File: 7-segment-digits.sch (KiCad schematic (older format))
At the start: 0 parts

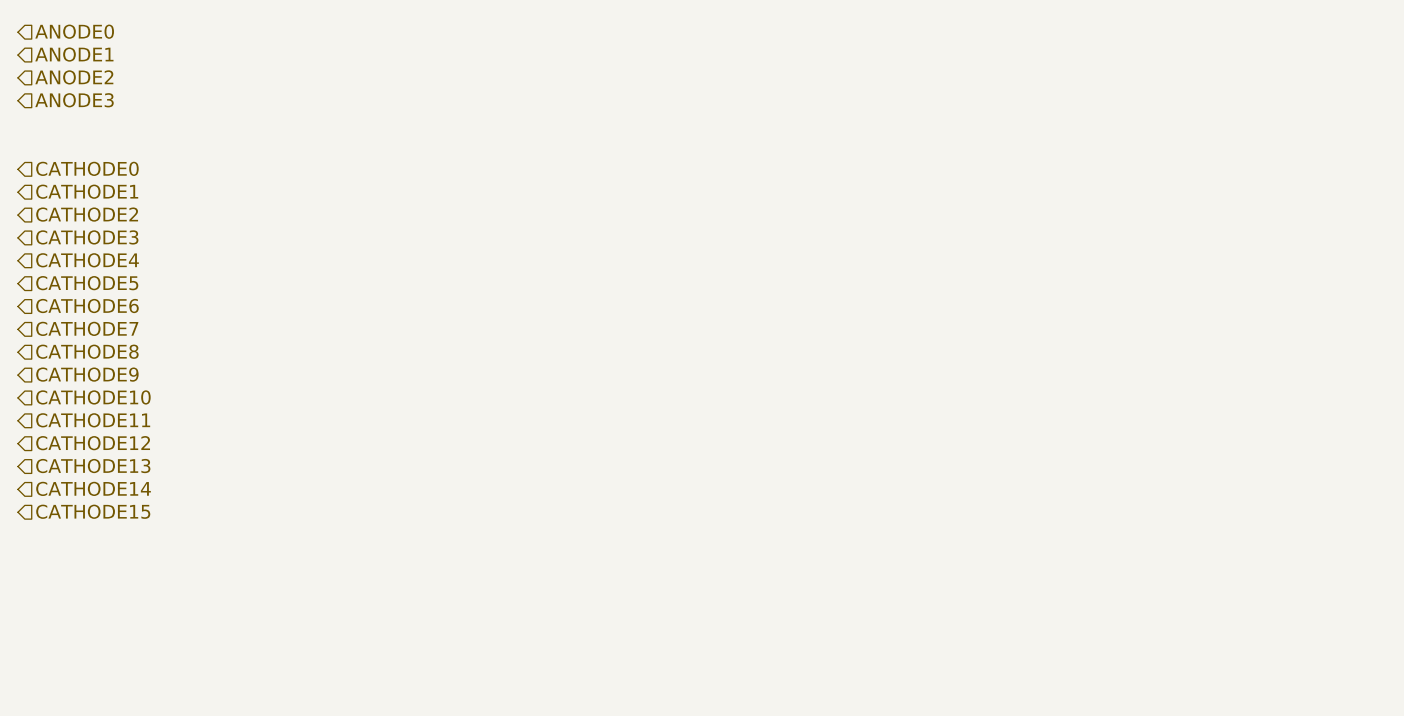
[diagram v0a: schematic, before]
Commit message: I think the layout is finished now. I'll check again after I sleep.
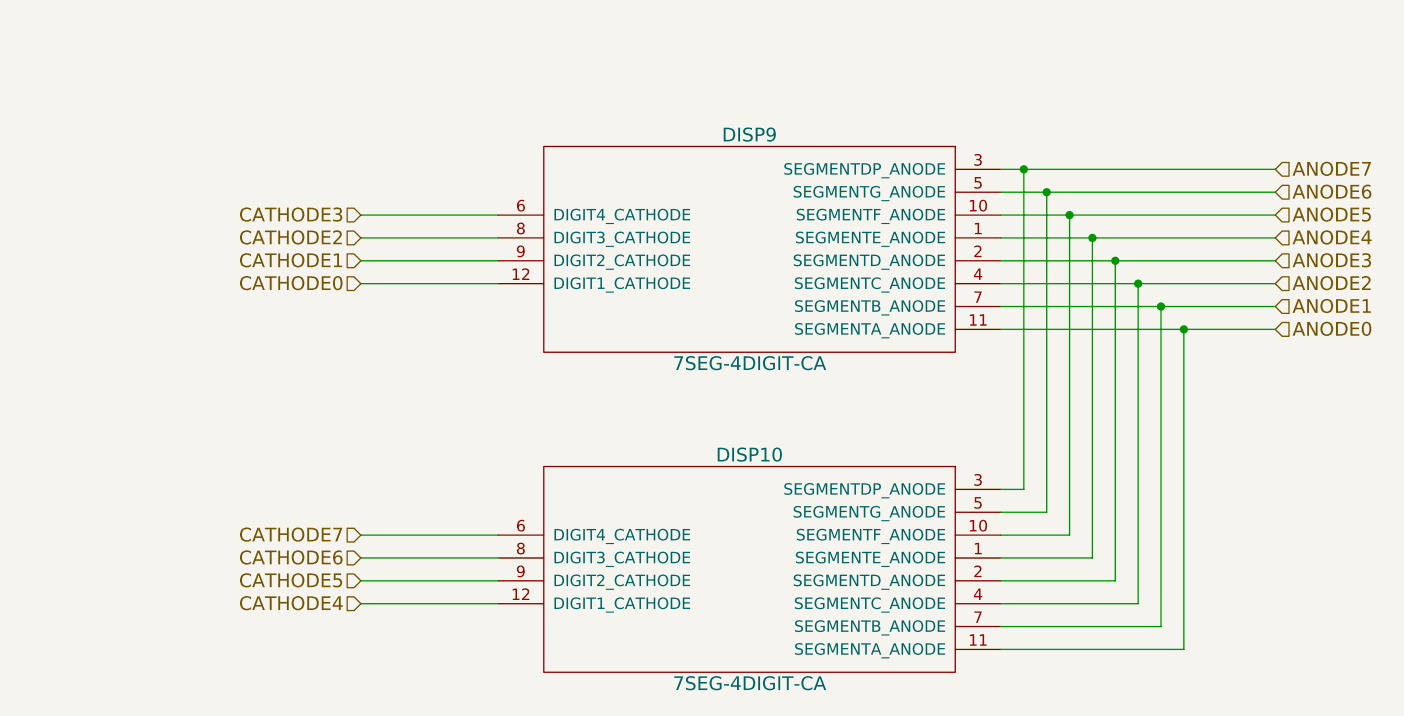
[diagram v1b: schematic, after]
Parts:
- added DISP10, DISP9: 7SEG-4DIGIT-CA, PinballParts:ATA8041, symbol 7SEG-4DIGIT-CA
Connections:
- net ANODE0: now also DISP10.11 (SEGMENTA_ANODE), DISP9.11 (SEGMENTA_ANODE)
- net ANODE1: now also DISP10.7 (SEGMENTB_ANODE), DISP9.7 (SEGMENTB_ANODE)
- net ANODE2: now also DISP10.4 (SEGMENTC_ANODE), DISP9.4 (SEGMENTC_ANODE)
- net ANODE3: now also DISP10.2 (SEGMENTD_ANODE), DISP9.2 (SEGMENTD_ANODE)
- net CATHODE0: now also DISP9.12 (DIGIT1_CATHODE)
- net CATHODE1: now also DISP9.9 (DIGIT2_CATHODE)
- net CATHODE2: now also DISP9.8 (DIGIT3_CATHODE)
- net CATHODE3: now also DISP9.6 (DIGIT4_CATHODE)
- net CATHODE4: now also DISP10.12 (DIGIT1_CATHODE)
- net CATHODE5: now also DISP10.9 (DIGIT2_CATHODE)
- net CATHODE6: now also DISP10.8 (DIGIT3_CATHODE)
- net CATHODE7: now also DISP10.6 (DIGIT4_CATHODE)
- new net ANODE4: DISP10.1 (SEGMENTE_ANODE), DISP9.1 (SEGMENTE_ANODE)
- new net ANODE5: DISP10.10 (SEGMENTF_ANODE), DISP9.10 (SEGMENTF_ANODE)
- new net ANODE6: DISP10.5 (SEGMENTG_ANODE), DISP9.5 (SEGMENTG_ANODE)
- new net ANODE7: DISP10.3 (SEGMENTDP_ANODE), DISP9.3 (SEGMENTDP_ANODE)
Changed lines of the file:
@@
 EESchema Schematic File Version 2
+LIBS:score-module-pcb-v1-rescue
 LIBS:power
 LIBS:device
@@
 LIBS:memory
 LIBS:xilinx
-LIBS:special
 LIBS:microcontrollers
 LIBS:dsp
@@
 Comment4 ""
 $EndDescr
-Text HLabel 2600 1800 2    60   Input ~ 0
+Text HLabel 8100 3100 2    60   Input ~ 0
 ANODE0
-Text HLabel 2600 1900 2    60   Input ~ 0
+Text HLabel 8100 3000 2    60   Input ~ 0
 ANODE1
-Text HLabel 2600 2000 2    60   Input ~ 0
+Text HLabel 8100 2900 2    60   Input ~ 0
 ANODE2
-Text HLabel 2600 2100 2    60   Input ~ 0
+Text HLabel 8100 2800 2    60   Input ~ 0
 ANODE3
-Text HLabel 2600 2400 2    60   Input ~ 0
+Text HLabel 4100 2900 0    60   Input ~ 0
 CATHODE0
-Text HLabel 2600 2500 2    60   Input ~ 0
+Text HLabel 4100 2800 0    60   Input ~ 0
 CATHODE1
-Text HLabel 2600 2600 2    60   Input ~ 0
+Text HLabel 4100 2700 0    60   Input ~ 0
 CATHODE2
-Text HLabel 2600 2700 2    60   Input ~ 0
+Text HLabel 4100 2600 0    60   Input ~ 0
 CATHODE3
-Text HLabel 2600 2800 2    60   Input ~ 0
+Text HLabel 4100 4300 0    60   Input ~ 0
 CATHODE4
-Text HLabel 2600 2900 2    60   Input ~ 0
+Text HLabel 4100 4200 0    60   Input ~ 0
 CATHODE5
-Text HLabel 2600 3000 2    60   Input ~ 0
+Text HLabel 4100 4100 0    60   Input ~ 0
 CATHODE6
-Text HLabel 2600 3100 2    60   Input ~ 0
+Text HLabel 4100 4000 0    60   Input ~ 0
 CATHODE7
-Text HLabel 2600 3200 2    60   Input ~ 0
-CATHODE8
-Text HLabel 2600 3300 2    60   Input ~ 0
-CATHODE9
-Text HLabel 2600 3400 2    60   Input ~ 0
-CATHODE10
-Text HLabel 2600 3500 2    60   Input ~ 0
-CATHODE11
-Text HLabel 2600 3600 2    60   Input ~ 0
-CATHODE12
-Text HLabel 2600 3700 2    60   Input ~ 0
-CATHODE13
-Text HLabel 2600 3800 2    60   Input ~ 0
-CATHODE14
-Text HLabel 2600 3900 2    60   Input ~ 0
-CATHODE15
+Text HLabel 8100 2700 2    60   Input ~ 0
+ANODE4
+Text HLabel 8100 2600 2    60   Input ~ 0
+ANODE5
+Text HLabel 8100 2500 2    60   Input ~ 0
+ANODE6
+Text HLabel 8100 2400 2    60   Input ~ 0
+ANODE7
+$Comp
+L 7SEG-4DIGIT-CA DISP9
+U 1 1 560EA1A5
+P 5800 2750
+F 0 "DISP9" H 5800 3250 60  0000 C CNN
+F 1 "7SEG-4DIGIT-CA" H 5800 2250 60  0000 C CNN
+F 2 "PinballParts:ATA8041" H 5800 2750 60  0001 C CNN
+F 3 "" H 5800 2750 60  0000 C CNN
+	1    5800 2750
+	1    0    0    -1
+$EndComp
+$Comp
+L 7SEG-4DIGIT-CA DISP10
+U 1 1 560EA1DC
+P 5800 4150
+F 0 "DISP10" H 5800 4650 60  0000 C CNN
+F 1 "7SEG-4DIGIT-CA" H 5800 3650 60  0000 C CNN
+F 2 "PinballParts:ATA8041" H 5800 4150 60  0001 C CNN
+F 3 "" H 5800 4150 60  0000 C CNN
+	1    5800 4150
+	1    0    0    -1
+$EndComp
+Wire Wire Line
+	8100 3100 6900 3100
+Wire Wire Line
+	6900 3000 8100 3000
+Wire Wire Line
+	8100 2900 6900 2900
+Wire Wire Line
+	6900 2800 8100 2800
+Wire Wire Line
+	8100 2700 6900 2700
+Wire Wire Line
+	6900 2600 8100 2600
+Wire Wire Line
+	8100 2500 6900 2500
+Wire Wire Line
+	6900 2400 8100 2400
+Wire Wire Line
+	6900 3800 7000 3800
+Wire Wire Line
+	7000 3800 7000 2400
+Connection ~ 7000 2400
+Wire Wire Line
+	6900 3900 7100 3900
+Wire Wire Line
+	7100 3900 7100 2500
+Connection ~ 7100 2500
+Wire Wire Line
+	7200 2600 7200 4000
+Wire Wire Line
+	7200 4000 6900 4000
+Connection ~ 7200 2600
+Wire Wire Line
+	6900 4100 7300 4100
+Wire Wire Line
+	7300 4100 7300 2700
+Connection ~ 7300 2700
+Wire Wire Line
+	7400 2800 7400 4200
+Wire Wire Line
+	7400 4200 6900 4200
+Connection ~ 7400 2800
+Wire Wire Line
+	6900 4300 7500 4300
+Wire Wire Line
+	7500 4300 7500 2900
+Connection ~ 7500 2900
+Wire Wire Line
+	6900 4400 7600 4400
+Wire Wire Line
+	7600 4400 7600 3000
+Connection ~ 7600 3000
+Wire Wire Line
+	6900 4500 7700 4500
+Wire Wire Line
+	7700 4500 7700 3100
+Connection ~ 7700 3100
+Wire Wire Line
+	4700 4300 4100 4300
+Wire Wire Line
+	4100 4200 4700 4200
+Wire Wire Line
+	4700 4100 4100 4100
+Wire Wire Line
+	4100 4000 4700 4000
+Wire Wire Line
+	4700 2900 4100 2900
+Wire Wire Line
+	4100 2800 4700 2800
+Wire Wire Line
+	4700 2700 4100 2700
+Wire Wire Line
+	4100 2600 4700 2600
 $EndSCHEMATC
